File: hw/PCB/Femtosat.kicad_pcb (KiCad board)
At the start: 2 copper layers, 35 parts, among them J1 USB_B_Micro, J2 Programmer, J3 SMA, J4 Battery, J5 Micro_SD_Card_Det, SW1 Reset_push, U0 SAMD21E, U1 AP7215-33YG-13, U2 AV4524, U3 RFM69HCW, U4 TRH-G2, U5 XA1110, Y1 32.768kHz

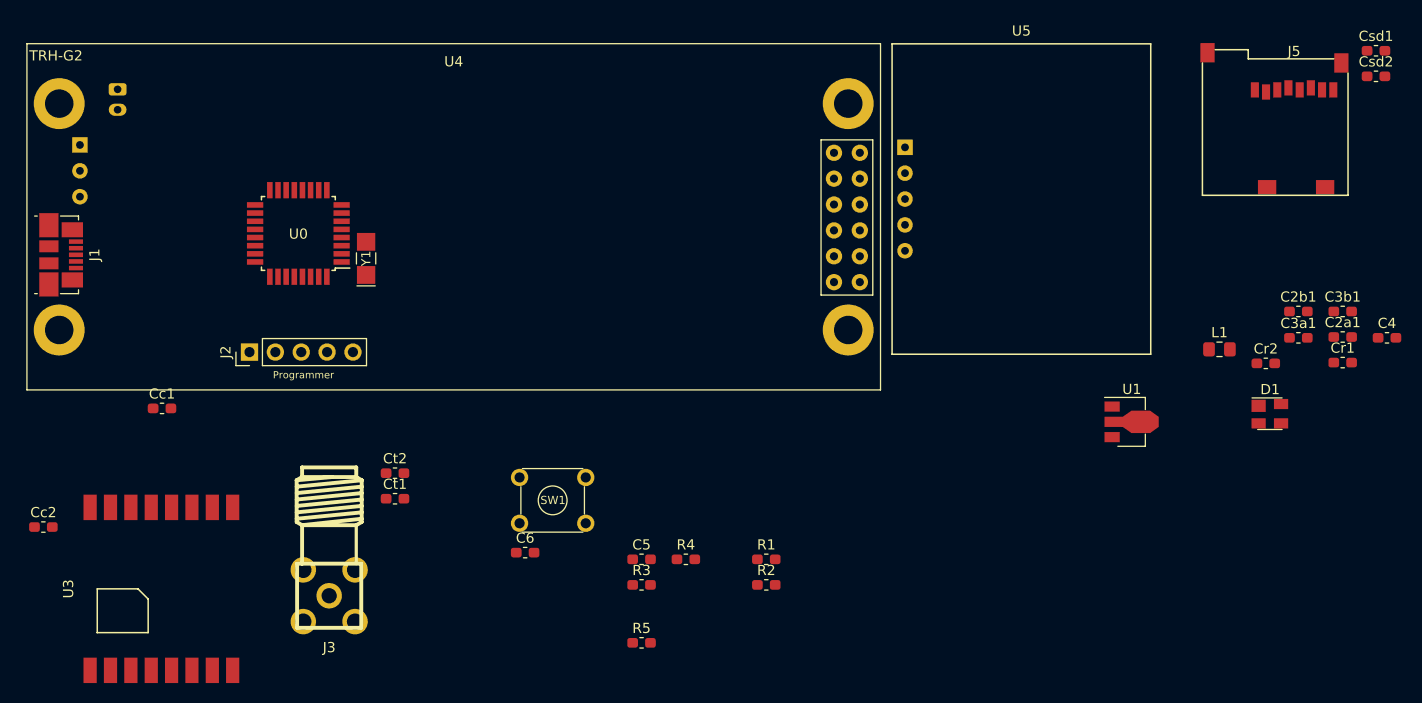
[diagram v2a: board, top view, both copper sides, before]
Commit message: Replaced a 100nF capacitor with a 10uF capacitor. Worked on PCB preliminary layout.
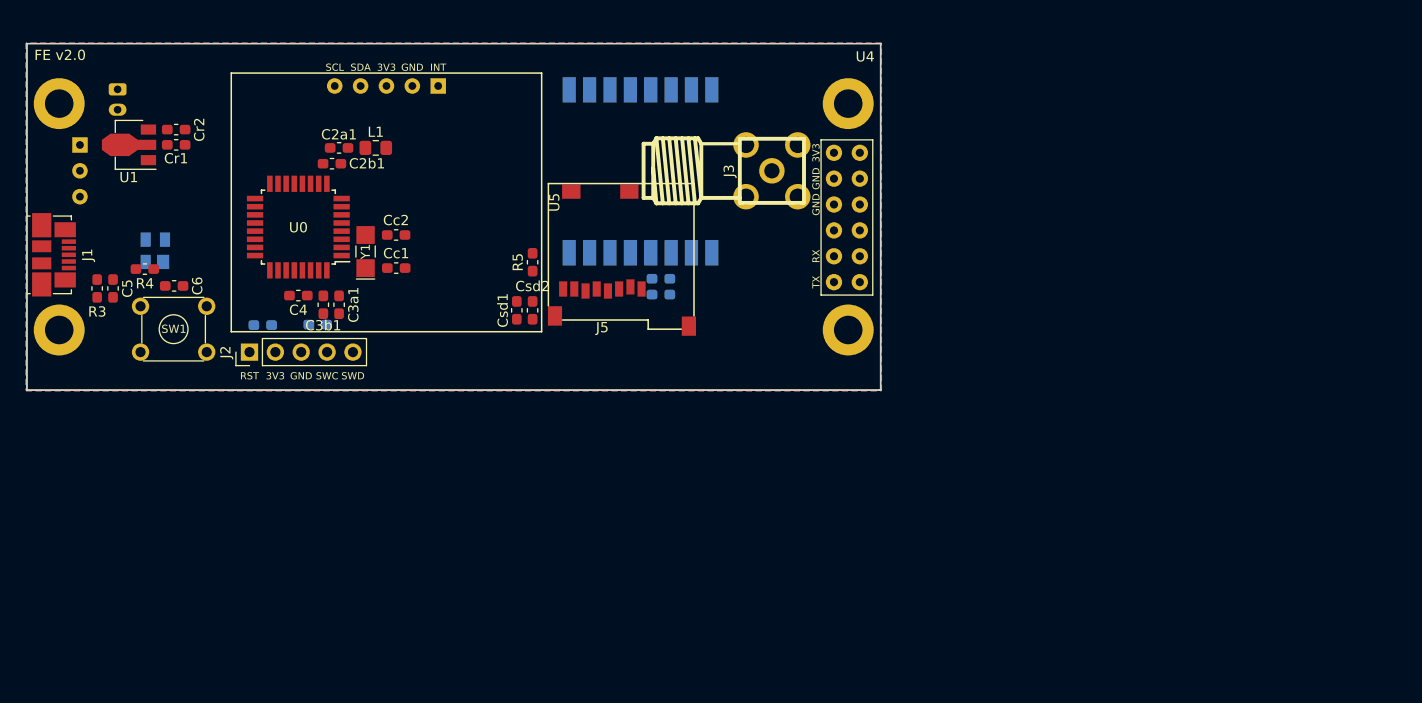
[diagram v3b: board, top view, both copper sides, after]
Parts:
- C3a1: value 100nF -> 10uF
- Ct1, Ct2, D1, R1, R2, U3: moved to B.Cu
- moved Cr1 116.5 mm to (100.5, 48.2)
- moved D1 110.6 mm to (98.5, 58.6), turned to 90 degrees
- moved Cr2 109.4 mm to (100.5, 46.8)
- moved C4 107.0 mm to (112.5, 63.0), turned to 180 degrees
- moved U1 101.3 mm to (96.3, 48.2), turned to 180 degrees
- moved C2a1 100.3 mm to (116.5, 48.5), turned to 180 degrees
- moved C3b1 100.1 mm to (115.0, 64.0), turned to 270 degrees
- moved C2b1 96.0 mm to (115.8, 50.1), turned to 180 degrees
- moved C3a1 94.3 mm to (116.5, 64.0), turned to 270 degrees
- moved Csd1 88.1 mm to (134.0, 64.5), turned to 270 degrees
- moved Csd2 85.9 mm to (135.6, 64.5), turned to 270 degrees
- moved L1 85.2 mm to (120.2, 48.5)
- moved J5 68.0 mm to (142.4, 53.5), turned to 180 degrees
- moved U3 62.4 mm to (146.2, 50.9), turned to 270 degrees
- moved U5 62.4 mm to (121.2, 53.9), turned to 270 degrees
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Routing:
- added copper zone on B.Cu, net GND
- added copper zone on F.Cu, net GND
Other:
- board outline added: 83.8 x 34 mm
- board text added: "+"
- board text added: "-"
- board text added: "3V3"
- board text added: "FE v2.0"
- board text added: "GND"
- board text added: "INT"
- board text added: "RST"
- board text added: "RX"
- board text added: "SCL"
- board text added: "SDA"
- board text added: "SWC"
- board text added: "SWD"
- board text added: "TX"

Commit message: Ended preliminary design phase.
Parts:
- moved Csd1 30.4 mm to (156.4, 44.0), turned to 90 degrees
- moved Csd2 28.2 mm to (154.9, 44.0), turned to 90 degrees
- moved R5 7.83 mm to (135.3, 52.0), turned to 180 degrees
- moved J5 4.41 mm to (146.1, 56.0), turned to 0 degrees
- moved R4 4.19 mm to (93.3, 60.1)
- moved D1 1.50 mm to (100.0, 58.6)
- moved C4 1.41 mm to (112.2, 64.4)
- moved C3a1 1.10 mm to (116.5, 65.0)
- moved C3b1 1.10 mm to (114.9, 65.0)
- moved C5 0.43 mm to (94.0, 62.6), turned to 90 degrees
- moved R3 0.42 mm to (92.5, 62.6), turned to 90 degrees
- turned R2 to 180 degrees
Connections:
- U0 pad 11: /GPS_INT -> Net-(U0-Pad11)
- U0 pad 12: /SD_CD -> /GPS_INT
- U4 pad : (no net) -> GND
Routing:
- net +3V3: track 0.00 -> 160.2 mm, vias 0 -> 9
- net /RX: track 0.00 -> 86.4 mm, vias 0 -> 3
- net GND: track 0.00 -> 86.1 mm, vias 0 -> 25
- net /TX: track 0.00 -> 75.3 mm, vias 0 -> 3
- net /MISO: track 0.00 -> 72.5 mm, vias 0 -> 4
- net /SCK: track 0.00 -> 60.4 mm, vias 0 -> 5
- net /TRX_NSS: track 0.00 -> 59.3 mm, vias 0 -> 1
- net /TRX_RST: track 0.00 -> 55.6 mm, vias 0 -> 5
- net /TRX_INT: track 0.00 -> 47.5 mm, vias 0 -> 3
- net /MOSI: track 0.00 -> 44.7 mm, vias 0 -> 3
- net /DL_NSS: track 0.00 -> 29.9 mm
- net /SCL: track 0.00 -> 28.9 mm, vias 0 -> 1
- net /DL_CD: track 0.00 -> 28.3 mm
- net /SDA: track 0.00 -> 28.1 mm, vias 0 -> 1
- net /USB/SHIELD: track 0.00 -> 25.0 mm, vias 0 -> 1
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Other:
- net class Default: via_dia 1.6 -> 1.4; via_drill 0.7 -> 0.5
- net class Power: via_dia 1.6 -> 1.4; via_drill 0.7 -> 0.5
- net class USB: via_dia 1.6 -> 1.4; via_drill 0.7 -> 0.5
- net class uC: via_dia 1.6 -> 1.3; via_drill 0.7 -> 0.4

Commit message: Final revision check. Generated the Gerber files.
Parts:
- J3: value SMA -> U.FL; footprint Antenna:SMA -> Connector_Coaxial:U.FL_Hirose_U.FL-R-SMT-1_Vertical; moved to B.Cu
- moved J3 8.21 mm to (157.4, 58.9), turned to 0 degrees
- moved J4 0.80 mm to (94.0, 42.8)
- moved U2 0.45 mm to (90.7, 50.8)
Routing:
- net GND: track 86.1 -> 132.5 mm, vias 25 -> 36
- net /Communication/ANT: track 11.3 -> 3.25 mm
- net /VUSB: track 24.1 -> 19.1 mm
